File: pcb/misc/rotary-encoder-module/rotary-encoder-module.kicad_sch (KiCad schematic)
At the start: 13 parts, among them J1 JST SH, J2 Pin headers, SW1 RotaryEncoder_Switch_MP

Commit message: Rename `connectors` symbol and footprint libraries to `connector`
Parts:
- J1: footprint connectors:JST_SH_SM05B-SRSS-TB_1x05-1MP_P1.00mm_Horizontal -> connector:JST_SH_SM05B-SRSS-TB_1x05-1MP_P1.00mm_Horizontal
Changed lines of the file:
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@@
 			)
 		)
-		(property "Footprint" "connectors:JST_SH_SM05B-SRSS-TB_1x05-1MP_P1.00mm_Horizontal"
+		(property "Footprint" "connector:JST_SH_SM05B-SRSS-TB_1x05-1MP_P1.00mm_Horizontal"
 			(at 86.36 171.45 0)
 			(effects

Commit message: Migrate rotary encoder footprints from `custom` to `electromechanical`
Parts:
- SW1: footprint custom:RotaryEncoder_Alps_EC11E-Switch_Vertical_H20mm -> electromechanical:RotaryEncoder_Alps_EC11E-Switch_Vertical_H20mm
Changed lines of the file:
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@@
 			)
 		)
-		(property "Footprint" "custom:RotaryEncoder_Alps_EC11E-Switch_Vertical_H20mm"
+		(property "Footprint" "electromechanical:RotaryEncoder_Alps_EC11E-Switch_Vertical_H20mm"
 			(at 140.97 83.566 0)
 			(effects

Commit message: Migrate 0603 capacitor hand soldering footprint to `discrete`
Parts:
- C1, C2, C3: footprint custom:C_0603_1608Metric_Pad1.08x0.95mm_HandSolder -> discrete:C_0603_1608Metric_Pad1.08x0.95mm_HandSolder
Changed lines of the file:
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@@
 			)
 		)
-		(property "Footprint" "custom:C_0603_1608Metric_Pad1.08x0.95mm_HandSolder"
+		(property "Footprint" "discrete:C_0603_1608Metric_Pad1.08x0.95mm_HandSolder"
 			(at 111.76 95.25 0)
 			(effects
@@
 			)
 		)
-		(property "Footprint" "custom:C_0603_1608Metric_Pad1.08x0.95mm_HandSolder"
+		(property "Footprint" "discrete:C_0603_1608Metric_Pad1.08x0.95mm_HandSolder"
 			(at 121.92 95.25 0)
 			(effects
@@
 			)
 		)
-		(property "Footprint" "custom:C_0603_1608Metric_Pad1.08x0.95mm_HandSolder"
+		(property "Footprint" "discrete:C_0603_1608Metric_Pad1.08x0.95mm_HandSolder"
 			(at 86.36 146.05 0)
 			(effects

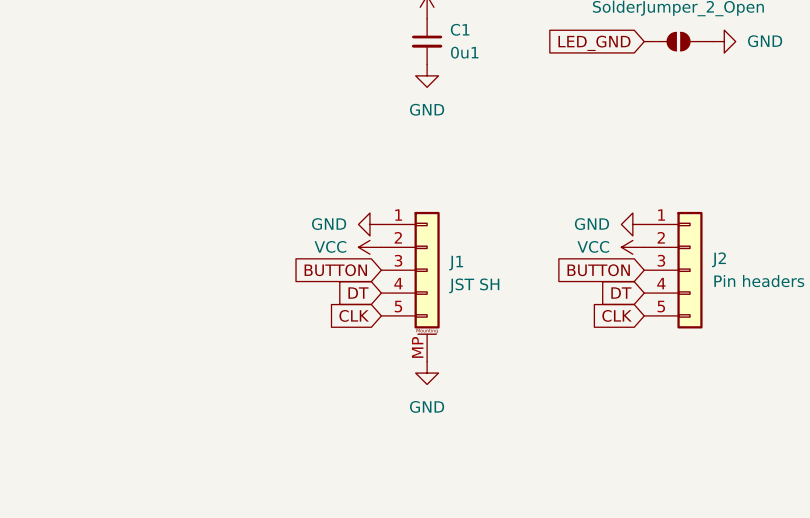
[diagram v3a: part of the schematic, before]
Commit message: Use new JST SH rotary encoder connector symbol in rotary encoder module
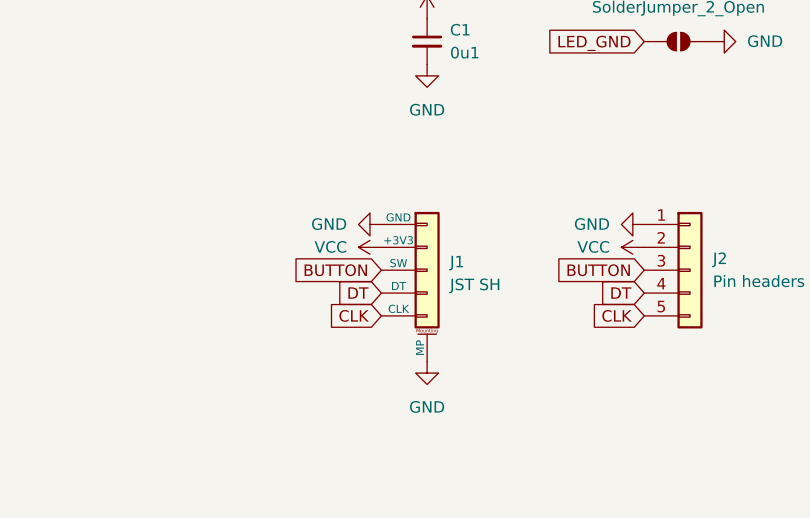
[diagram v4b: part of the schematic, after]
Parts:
- removed J1: JST SH, connector:JST_SH_SM05B-SRSS-TB_1x05-1MP_P1.00mm_Horizontal, symbol Connector_Generic_MountingPin:Conn_01x05_MountingPin
- added J1: JST SH, connector:JST_SH_SM05B-SRSS-TB_1x05-1MP_P1.00mm_Horizontal, symbol connector:JST_SH_01x05_RotaryEncoder
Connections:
- net BUTTON: now also J1.3 (SW)
- net CLK: now also J1.5 (CLK)
- net DT: now also J1.4 (DT)
- net GND: now also J1.1 (GND), J1.MP
- net VCC: now also J1.2 (+3V3)
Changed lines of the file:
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@@
-	)
-	(symbol
-		(lib_id "Connector_Generic_MountingPin:Conn_01x05_MountingPin")
-		(at 86.36 171.45 0)
-		(unit 1)
-		(exclude_from_sim no)
-		(in_bom yes)
-		(on_board yes)
-		(dnp no)
-		(fields_autoplaced yes)
-		(property "Reference" "J1"
-			(at 88.9 170.5355 0)
-			(effects
-				(font
-					(size 1.27 1.27)
-				)
-				(justify left)
-			)
-		)
-		(property "Value" "JST SH"
-			(at 88.9 173.0755 0)
-			(effects
-				(font
-					(size 1.27 1.27)
-				)
-				(justify left)
-			)
-		)
-		(property "Footprint" "connector:JST_SH_SM05B-SRSS-TB_1x05-1MP_P1.00mm_Horizontal"
-			(at 86.36 171.45 0)
-			(effects
-				(font
-					(size 1.27 1.27)
-				)
-				(hide yes)
-			)
-		)
-		(property "Datasheet" "~"
-			(at 86.36 171.45 0)
-			(effects
-				(font
-					(size 1.27 1.27)
-				)
-				(hide yes)
-			)
-		)
-		(property "Description" "Generic connectable mounting pin connector, single row, 01x05, script generated (kicad-library-utils/schlib/autogen/connector/)"
-			(at 86.36 171.45 0)
-			(effects
-				(font
-					(size 1.27 1.27)
-				)
-				(hide yes)
-			)
-		)
-		(pin "MP"
-		)
-		(pin "1"
-		)
-		(pin "3"
-		)
-		(pin "4"
-		)
-		(pin "5"
-		)
-		(pin "2"
-		)
-		(instances
-			(project ""
-				(path "/76a56607-25e2-40a3-9282-ff279b153f75"
-					(reference "J1")
-					(unit 1)
-				)
-			)
-		)
 	)
 	(symbol
@@
 					(unit 1)
 				)
+			)
+		)
+	)
+	(symbol
+		(lib_id "connector:JST_SH_01x05_RotaryEncoder")
+		(at 86.36 171.45 0)
+		(unit 1)
+		(exclude_from_sim no)
+		(in_bom yes)
+		(on_board yes)
+		(dnp no)
+		(fields_autoplaced yes)
+		(property "Reference" "J1"
+			(at 88.9 170.5355 0)
+			(effects
+				(font
+					(size 1.27 1.27)
+				)
+				(justify left)
+			)
+		)
+		(property "Value" "JST SH"
+			(at 88.9 173.0755 0)
+			(effects
+				(font
+					(size 1.27 1.27)
+				)
+				(justify left)
+			)
+		)
+		(property "Footprint" "connector:JST_SH_SM05B-SRSS-TB_1x05-1MP_P1.00mm_Horizontal"
+			(at 86.36 171.45 0)
+			(effects
+				(font
+					(size 1.27 1.27)
+				)
+				(hide yes)
+			)
+		)
+		(property "Datasheet" "~"
+			(at 86.36 171.45 0)
+			(effects
+				(font
+					(size 1.27 1.27)
+				)
+				(hide yes)
+			)
+		)
+		(property "Description" "JST SH connector for rotary encoder"
+			(at 86.36 171.45 0)
+			(effects
+				(font
+					(size 1.27 1.27)
+				)
+				(hide yes)
+			)
+		)
+		(property "LCSC Part" "C7433426"
+			(at 86.36 171.45 0)
+			(effects
+				(font
+					(size 1.27 1.27)
+				)
+				(hide yes)
+			)
+		)
+		(pin "1"
+		)
+		(pin "2"
+		)
+		(pin "3"
+		)
+		(pin "MP"
+		)
+		(pin "5"
+		)
+		(pin "4"
+		)
+		(instances
+			(project ""
+				(path "/76a56607-25e2-40a3-9282-ff279b153f75"
+					(reference "J1")
+					(unit 1)
+				)

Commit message: Invert LED logic on rotary-encoder-module, update to v2
This also changes the solder jumpers to bridged by default
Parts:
- removed JP1, JP2: SolderJumper_2_Open, custom:SolderJumper-2_P1.0mm_Open_Pad, symbol Jumper:SolderJumper_2_Open
- added JP1, JP2: SolderJumper_2_Bridged, Jumper:SolderJumper-2_P1.3mm_Bridged_RoundedPad1.0x1.5mm, symbol Jumper:SolderJumper_2_Bridged
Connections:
- net BUTTON: now also JP1.1 (A)
- net VCC: now also JP2.1 (A)
- net at RN1.2 (R2.1): now also JP1.2 (B)
- net at RN2.8 (R1.2): now also LED1.1 (K); no longer LED1.2 (A)
- net at RN2.7 (R2.2): now also LED2.1 (K); no longer LED2.2 (A)
- net at RN2.6 (R3.2): now also LED3.1 (K); no longer LED3.2 (A)
- removed net LED_GND: LED1.1 (K), LED2.1 (K), LED3.1 (K)
- new net LED_VCC: JP2.2 (B), LED1.2 (A), LED2.2 (A), LED3.2 (A)

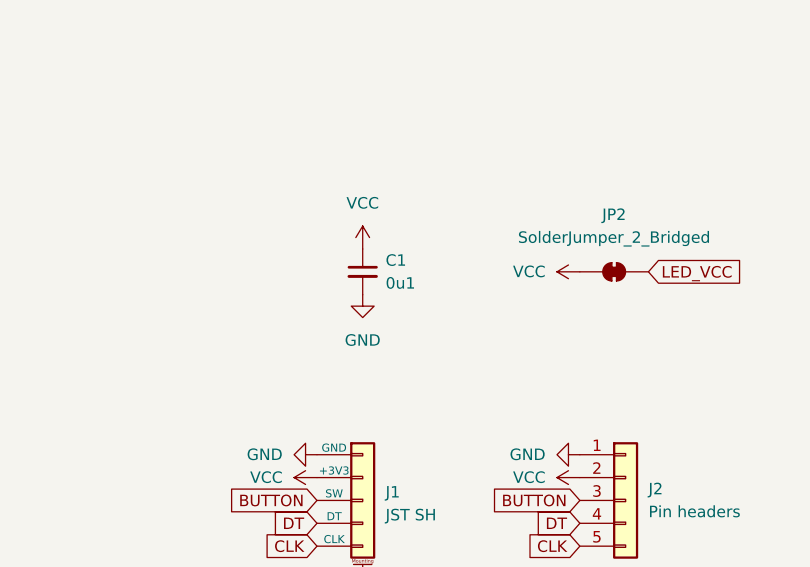
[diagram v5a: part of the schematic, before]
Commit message: Change C1 value to 1u
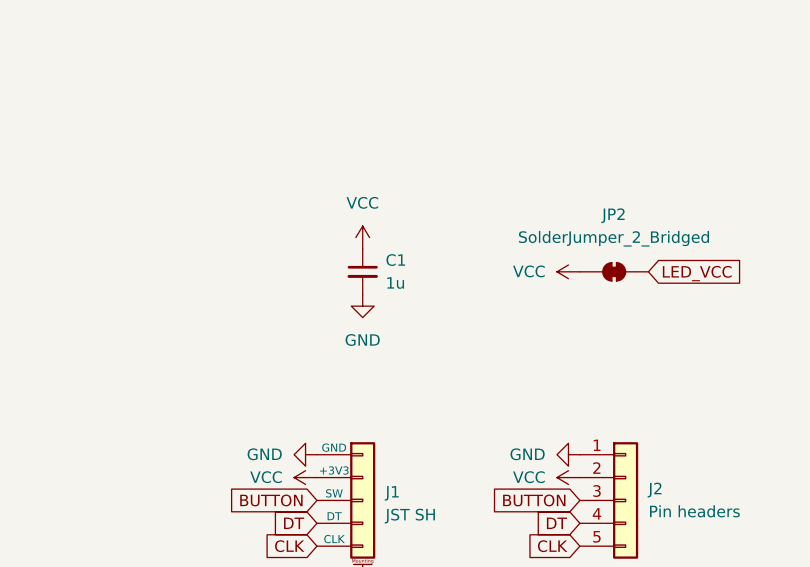
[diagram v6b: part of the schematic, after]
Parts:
- C1: value 0u1 -> 1u
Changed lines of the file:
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@@
 			)
 		)
-		(property "Value" "0u1"
+		(property "Value" "1u"
 			(at 88.9 147.3262 0)
 			(effects

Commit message: Use `discrete` resistor array footprints
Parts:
- RN1, RN2: footprint Resistor_SMD:R_Array_Convex_4x0603 -> discrete:R_Array_Convex_4x0603
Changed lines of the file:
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@@
 			)
 		)
-		(property "Footprint" "Resistor_SMD:R_Array_Convex_4x0603"
+		(property "Footprint" "discrete:R_Array_Convex_4x0603"
 			(at 109.728 78.74 90)
 			(effects
@@
 			)
 		)
-		(property "Footprint" "Resistor_SMD:R_Array_Convex_4x0603"
+		(property "Footprint" "discrete:R_Array_Convex_4x0603"
 			(at 157.988 71.12 90)
 			(effects
@@
 			)
 		)
-		(property "Footprint" "Resistor_SMD:R_Array_Convex_4x0603"
+		(property "Footprint" "discrete:R_Array_Convex_4x0603"
 			(at 119.888 78.74 90)
 			(effects
@@
 			)
 		)
-		(property "Footprint" "Resistor_SMD:R_Array_Convex_4x0603"
+		(property "Footprint" "discrete:R_Array_Convex_4x0603"
 			(at 83.058 76.2 90)
 			(effects
@@
 			)
 		)
-		(property "Footprint" "Resistor_SMD:R_Array_Convex_4x0603"
+		(property "Footprint" "discrete:R_Array_Convex_4x0603"
 			(at 171.45 101.092 90)
 			(effects
@@
 			)
 		)
-		(property "Footprint" "Resistor_SMD:R_Array_Convex_4x0603"
+		(property "Footprint" "discrete:R_Array_Convex_4x0603"
 			(at 171.45 112.522 90)
 			(effects
@@
 			)
 		)
-		(property "Footprint" "Resistor_SMD:R_Array_Convex_4x0603"
+		(property "Footprint" "discrete:R_Array_Convex_4x0603"
 			(at 187.198 74.93 90)
 			(effects
@@
 			)
 		)
-		(property "Footprint" "Resistor_SMD:R_Array_Convex_4x0603"
+		(property "Footprint" "discrete:R_Array_Convex_4x0603"
 			(at 97.028 76.2 90)
 			(effects
